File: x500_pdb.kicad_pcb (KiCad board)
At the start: 4 copper layers, 50 x 50 mm, 33 parts, among them IC1 LM21305SQ_NOPB, J1 Conn_01x02, J2 Conn_01x02, J3 Conn_01x02, J4 Conn_01x02

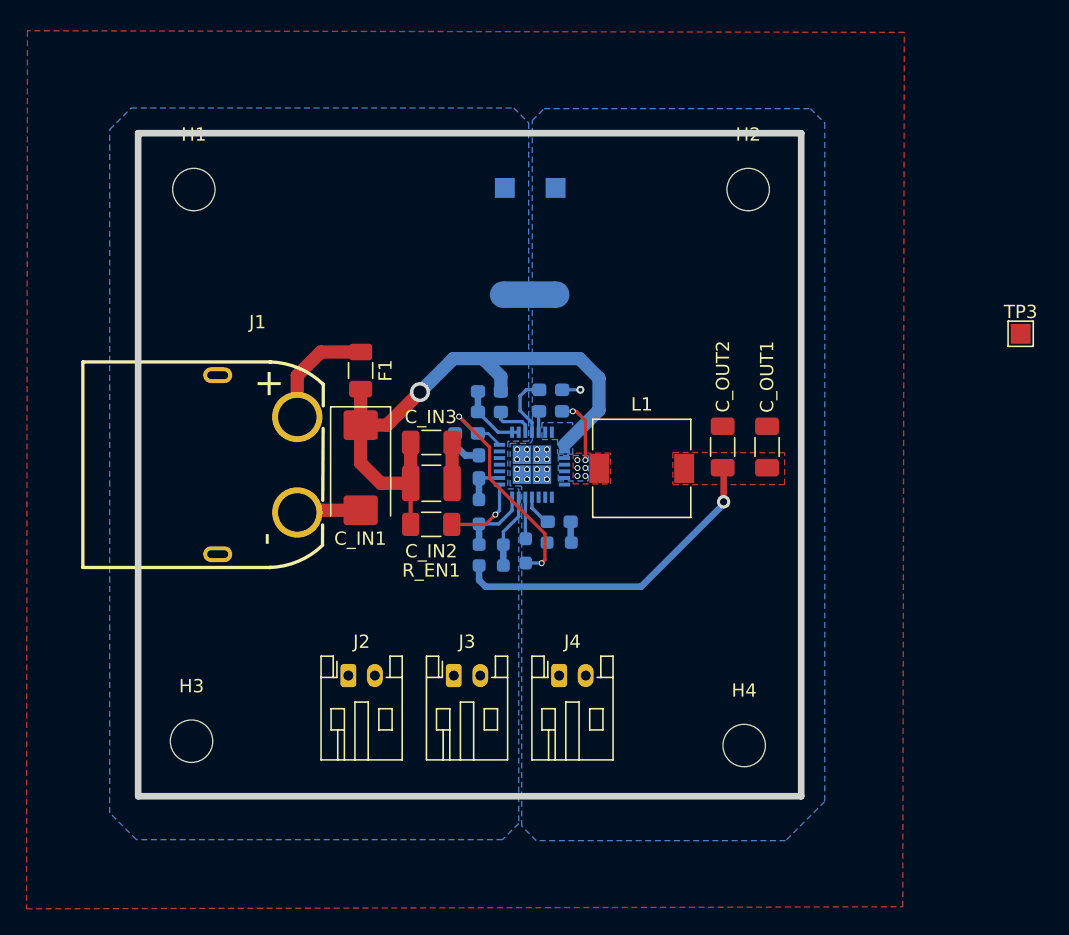
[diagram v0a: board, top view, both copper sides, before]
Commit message: 1.0-RC1. Need to move input caps closer
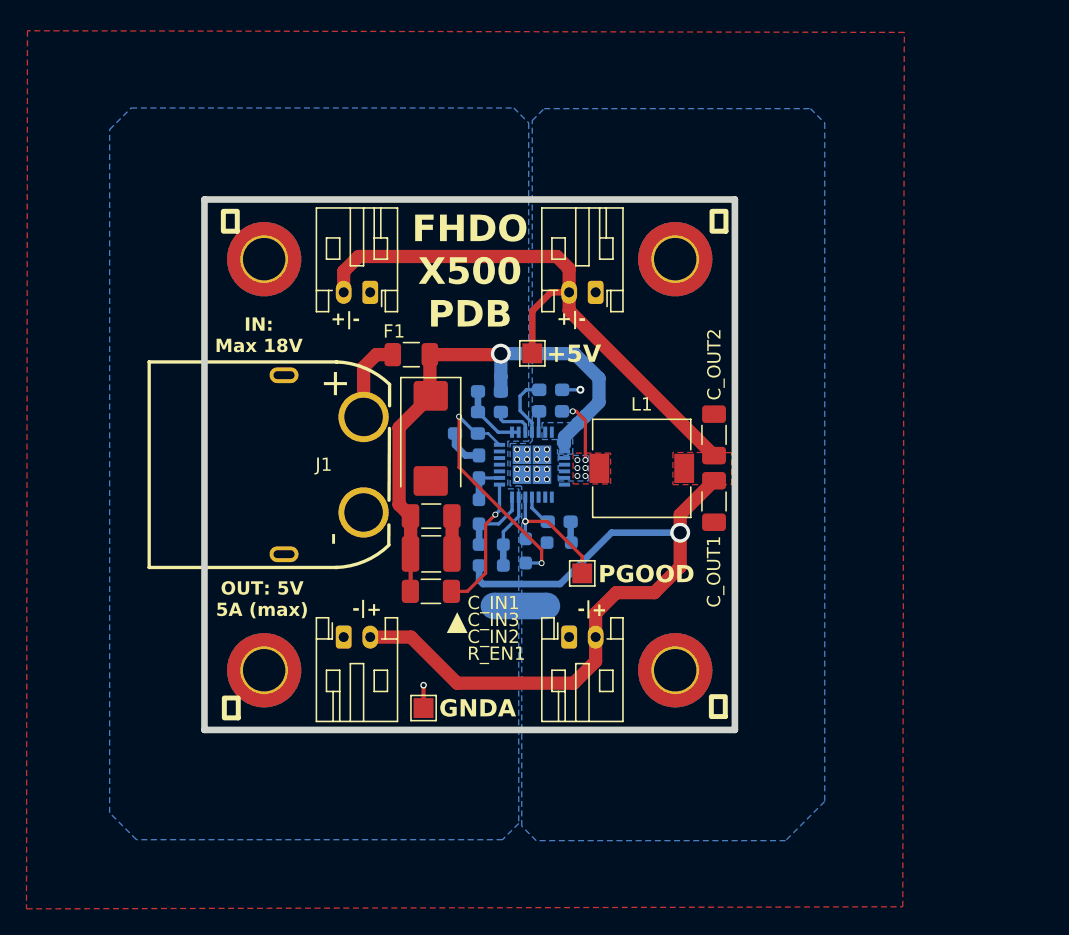
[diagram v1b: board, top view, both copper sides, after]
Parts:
- added J5: Conn_01x02, Connector_JST:JST_PH_S2B-PH-K_1x02_P2.00mm_Horizontal, F.Cu at (117.5, 92.0)
- H1, H2, H3, H4: footprint MountingHole:MountingHole_3.2mm_M3 -> MountingHole:MountingHole_3.2mm_M3_DIN965_Pad_TopBottom
- TP1, TP2: moved to F.Cu
- moved TP1 40.5 mm to (121.5, 123.4)
- moved TP3 37.7 mm to (133.5, 113.2)
- moved J4 29.0 mm to (134.5, 92.0), turned to 180 degrees
- moved NT1 23.5 mm to (128.8, 115.7)
- moved TP2 12.6 mm to (129.7, 96.6)
- moved J3 9.17 mm to (132.5, 118.0)
- moved H4 7.70 mm to (140.5, 120.5)
- moved H3 7.65 mm to (109.5, 120.5)
- moved H2 7.60 mm to (140.5, 89.5)
- moved H1 7.46 mm to (109.5, 89.5)
- moved C_OUT1 5.74 mm to (143.4, 107.8), turned to 90 degrees
- moved C_IN1 5.73 mm to (122.1, 103.0)
- moved C_IN3 5.55 mm to (122.1, 108.9)
- moved C_IN2 5.33 mm to (122.1, 111.7)
- moved R_EN1 5.05 mm to (122.1, 114.5)
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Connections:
- TP1 pad 1: GND -> GNDA
- TP2 pad 1: GNDA -> VOUT_5V
- TP3 pad 1: unconnected-(TP3-Pad1) -> /PGOOD
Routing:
- net VOUT_5V: track 25.1 -> 100.8 mm
- net /PGOOD: track 3.15 -> 9.81 mm, vias 0 -> 1
- net GND: track 9.29 -> 4.24 mm
- net BAT+_FUSED: track 46.5 -> 41.8 mm
- net /EN: track 5.99 -> 10.3 mm
- net +BATT: track 8.64 -> 6.34 mm
- net GNDA: track 11.6 -> 13.4 mm, vias 0 -> 1
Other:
- board size 50 x 50 mm -> 40 x 40 mm
- board text added: "+5V"
- board text added: "+|-"
- board text added: "FHDO FB4 NOV/25"
- board text added: "FHDO X500 PDB"
- board text added: "IN: Max 18V"
- board text added: "LM21305 Power Delivery Board"
- board text added: "OUT: 5V 5A (max)"
- board text added: "PGOOD"
- board text added: "Rosewick Reuter"
- board text added: "v1.0"
- board text added: "⏚"
- board text added: "▲"
- board text removed: "GND"

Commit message: 1.0-RC2 Moving input caps close to IC, rearranging components
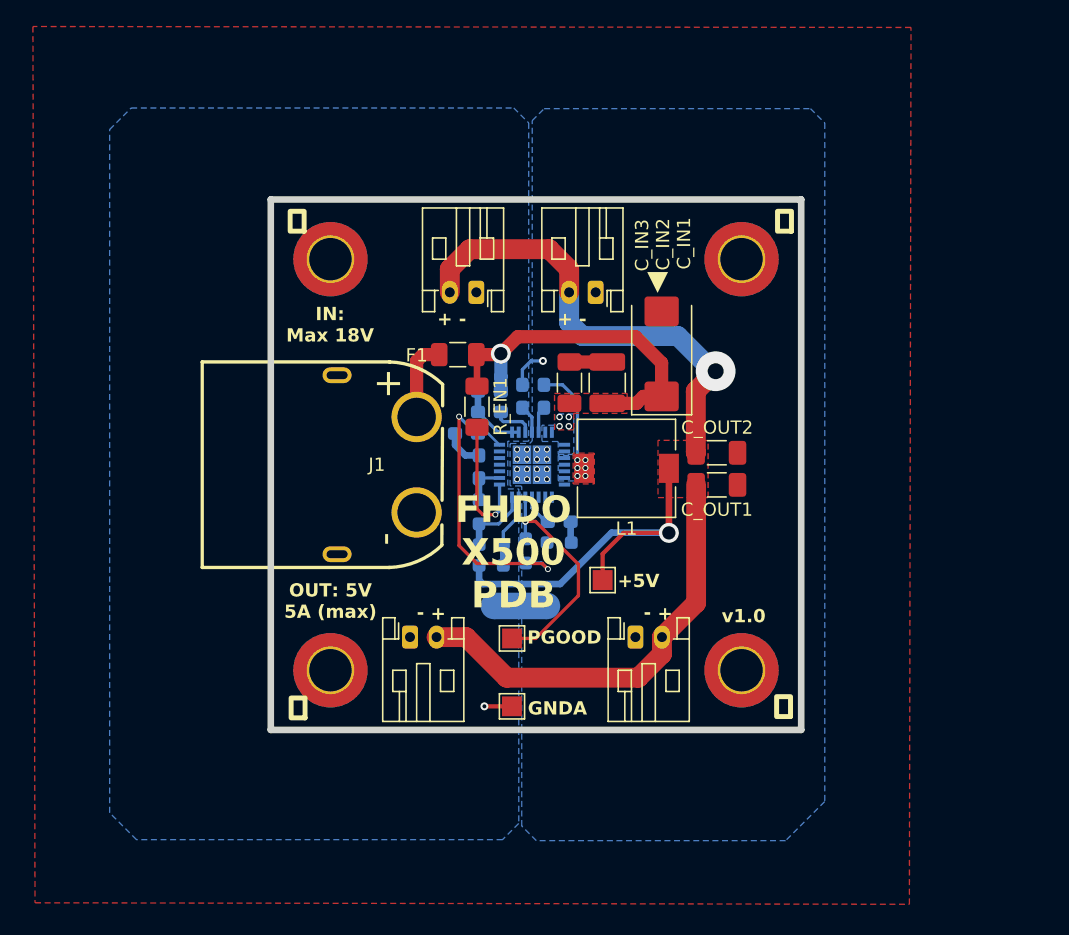
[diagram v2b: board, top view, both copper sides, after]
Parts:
- moved C_IN1 18.5 mm to (139.5, 96.6), turned to 90 degrees
- moved C_IN2 18.5 mm to (135.4, 98.8), turned to 90 degrees
- moved TP2 17.9 mm to (135.0, 113.7)
- moved C_IN3 14.5 mm to (132.5, 98.8), turned to 90 degrees
- moved R_EN1 14.4 mm to (125.5, 100.6), turned to -90 degrees
- moved J5 8.00 mm to (125.5, 92.0)
- moved TP3 7.22 mm to (128.2, 118.1)
- moved TP1 6.67 mm to (128.2, 123.2)
- moved H1 5.00 mm to (114.5, 89.5)
- moved H2 5.00 mm to (145.5, 89.5)
- moved H3 5.00 mm to (114.5, 120.5)
- moved H4 5.00 mm to (145.5, 120.5)
- moved J2 5.00 mm to (120.5, 118.0)
- moved J3 5.00 mm to (137.5, 118.0)
- moved J1 4.00 mm to (118.0, 105.0)
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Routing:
- net BAT+_FUSED: track 41.8 -> 27.4 mm, vias 1 -> 5
- net /PGOOD: track 9.81 -> 17.2 mm
- net /2V5: track 18.8 -> 23.0 mm
- net VOUT_5V: track 100.8 -> 97.9 mm, vias 1 -> 2
- net /5V0: track 4.74 -> 2.15 mm
- net /SW: track 5.03 -> 7.54 mm, vias 7 -> 6
- net GND: track 4.24 -> 5.82 mm
- added copper zone on F.Cu, net BAT+_FUSED
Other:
- board text added: "+ -"
- board text added: "GND"
- board text removed: "+|-"

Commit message: 1.0-RC2 Fixed Back Silkscreen
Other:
- outline, holes or cut-outs redrawn
- board text added: "▶"
- board text added: "▼"
- board text added: "◀"

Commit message: 1.0-RC3 Passing DRC
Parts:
- added J6: Conn_01x03, Connector_JST:JST_PH_S3B-PH-K_1x03_P2.00mm_Horizontal, F.Cu at (134.4, 91.3)
- J5: value Conn_01x02 -> Conn_01x03; footprint Connector_JST:JST_PH_S2B-PH-K_1x02_P2.00mm_Horizontal -> Connector_JST:JST_PH_S3B-PH-K_1x03_P2.00mm_Horizontal
- moved J4 27.3 mm to (129.0, 118.8), turned to 0 degrees
- moved TP1 10.9 mm to (122.9, 113.7)
- moved TP3 9.30 mm to (136.7, 114.4)
- moved TP2 2.57 mm to (136.7, 111.8)
- moved J5 0.86 mm to (126.0, 91.3)
- moved J2 0.75 mm to (120.5, 118.8)
- moved J3 0.75 mm to (137.5, 118.8)
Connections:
- J5 pad 2: VOUT_5V -> unconnected-(J5-Pin_2-Pad2)
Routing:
- net VOUT_5V: track 97.9 -> 73.2 mm
- net BAT+_FUSED: track 27.4 -> 47.1 mm
- net /PGOOD: track 17.2 -> 12.8 mm
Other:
- board text added: "+ | -"
- board text added: "- | +"
- board text added: "5V OUT"
- board text added: "BAT OUT"
- board text added: "BAT_FUSED"
- board text added: "Regulated 5V OUT"

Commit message: Remove unused via and trace
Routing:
- net VOUT_5V: track 73.2 -> 66.4 mm, vias 2 -> 1
